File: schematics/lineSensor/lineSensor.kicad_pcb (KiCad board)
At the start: 2 copper layers, 27 parts, among them P1 CONN_01X01, P2 CONN_01X01, P3 CONN_01X01, P4 CONN_01X01, P5 CONN_01X01, P6 CONN_01X01, P7 CONN_01X01

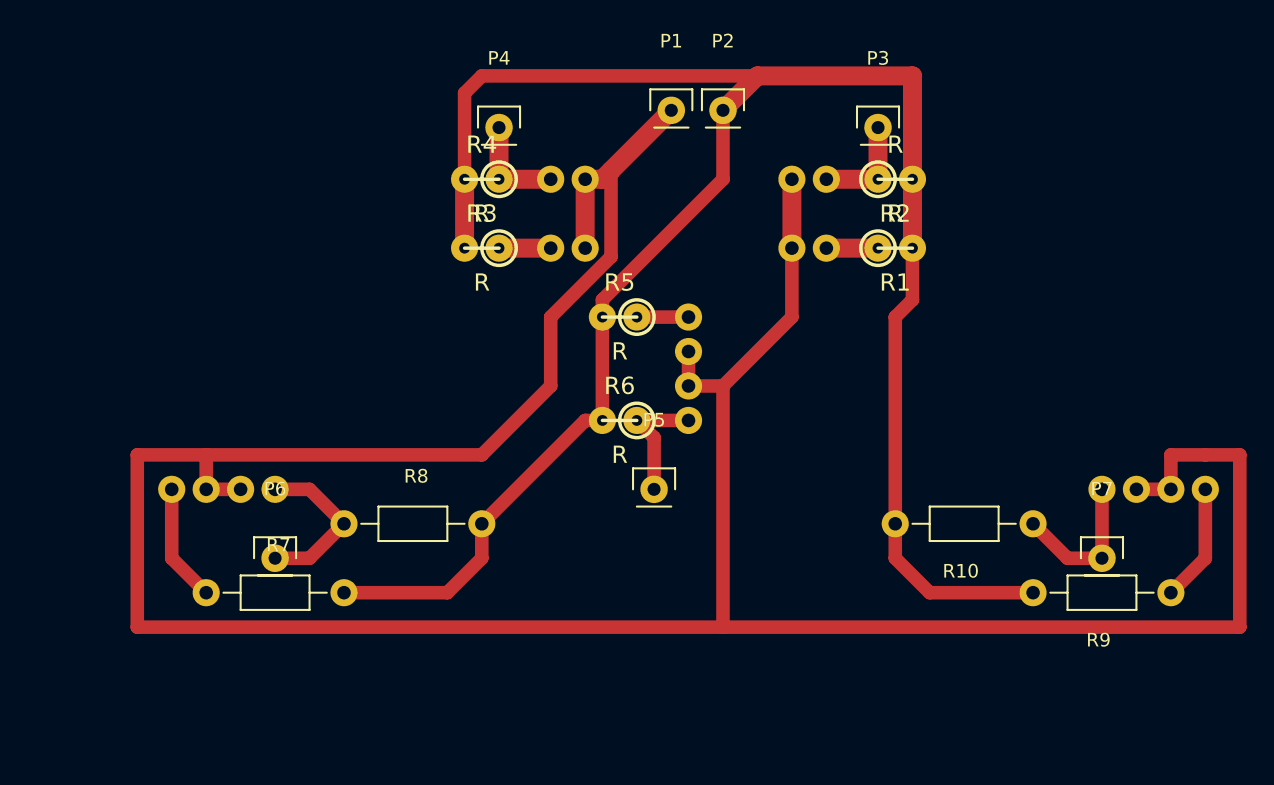
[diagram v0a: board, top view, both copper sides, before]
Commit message: Update schematic lineSensor and bug
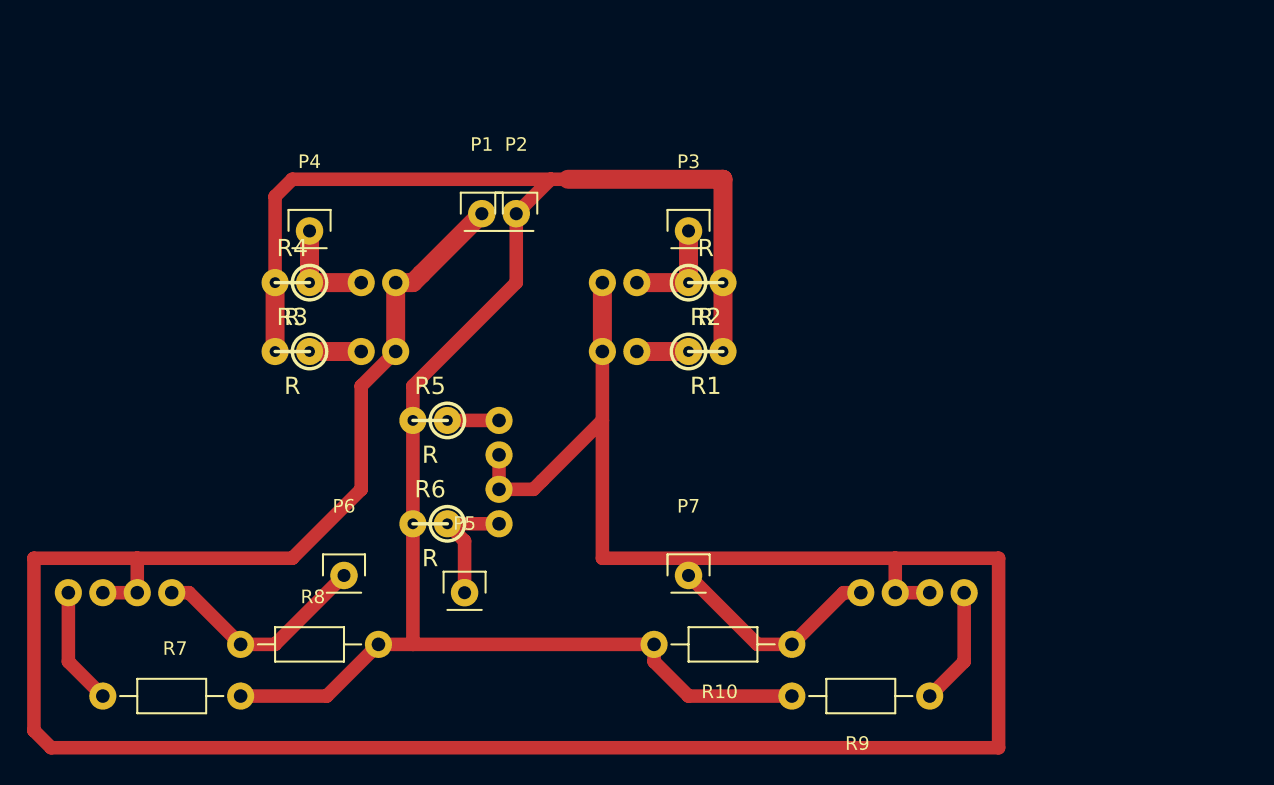
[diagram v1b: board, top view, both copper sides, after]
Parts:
- moved P7 30.5 mm to (157.5, 128.3)
- moved R10 19.9 mm to (165.1, 133.3)
- moved R9 19.3 mm to (175.3, 137.2)
- moved D10 19.3 mm to (170.2, 129.5)
- moved D9 19.3 mm to (177.8, 129.5)
- moved P2 17.0 mm to (144.8, 101.6)
- moved D1 15.9 mm to (153.7, 111.8)
- moved D2 15.9 mm to (153.7, 106.7)
- moved D3 15.9 mm to (133.3, 111.8)
- moved D4 15.9 mm to (133.3, 106.7)
- moved D5 15.9 mm to (143.5, 116.8)
- moved P3 15.9 mm to (157.5, 102.9)
- moved P4 15.9 mm to (129.5, 102.9)
- moved R1 15.9 mm to (158.8, 111.8)
- moved R2 15.9 mm to (158.8, 106.7)
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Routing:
- net Net-(P2-Pad1): track 148.2 -> 140.7 mm
- net Net-(D10-Pad1): track 11.2 -> 16.4 mm
- net Net-(D1-Pad2): track 226.0 -> 221.3 mm
- net Net-(D8-Pad1): track 12.3 -> 16.4 mm

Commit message: SCHEMATICS: group output pins
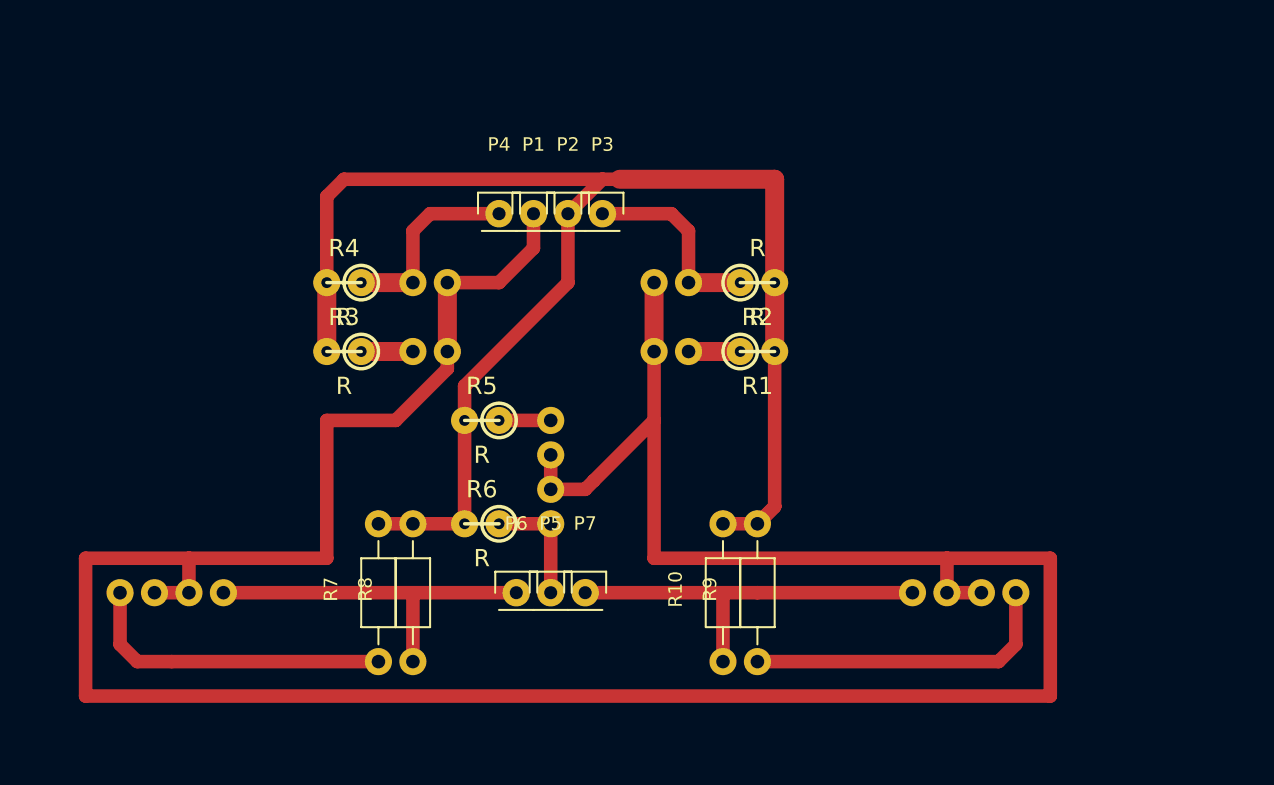
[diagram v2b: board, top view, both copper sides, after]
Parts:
- moved R7 20.5 mm to (134.6, 134.6), turned to 90 degrees
- moved P4 14.0 mm to (143.5, 101.6)
- moved R9 13.0 mm to (162.6, 134.6), turned to 90 degrees
- moved R8 12.8 mm to (137.2, 134.6), turned to 90 degrees
- moved P6 12.8 mm to (144.8, 129.5)
- moved P7 7.73 mm to (149.9, 129.5)
- moved P3 6.48 mm to (151.1, 101.6)
- moved P5 6.35 mm to (147.3, 129.5)
- moved R10 5.24 mm to (160.0, 134.6), turned to 90 degrees
- moved D1 3.81 mm to (157.5, 111.8)
- moved D10 3.81 mm to (174.0, 129.5)
- moved D2 3.81 mm to (157.5, 106.7)
- moved D3 3.81 mm to (137.2, 111.8)
- moved D4 3.81 mm to (137.2, 106.7)
- moved D5 3.81 mm to (147.3, 116.8)
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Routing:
- net Net-(P2-Pad1): track 140.7 -> 111.2 mm
- net Net-(D7-Pad1): track 8.67 -> 23.4 mm
- net Net-(D9-Pad1): track 8.67 -> 23.4 mm
- net Net-(D10-Pad1): track 16.4 -> 29.2 mm
- net Net-(D8-Pad1): track 16.4 -> 26.7 mm
- net Net-(D2-Pad1): track 7.62 -> 14.5 mm
- net Net-(D4-Pad1): track 7.62 -> 14.5 mm
- net Net-(D1-Pad2): track 221.3 -> 218.1 mm
- net Net-(D6-Pad1): track 9.42 -> 8.89 mm

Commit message: SCHEMATIC: update lineSensors and bug
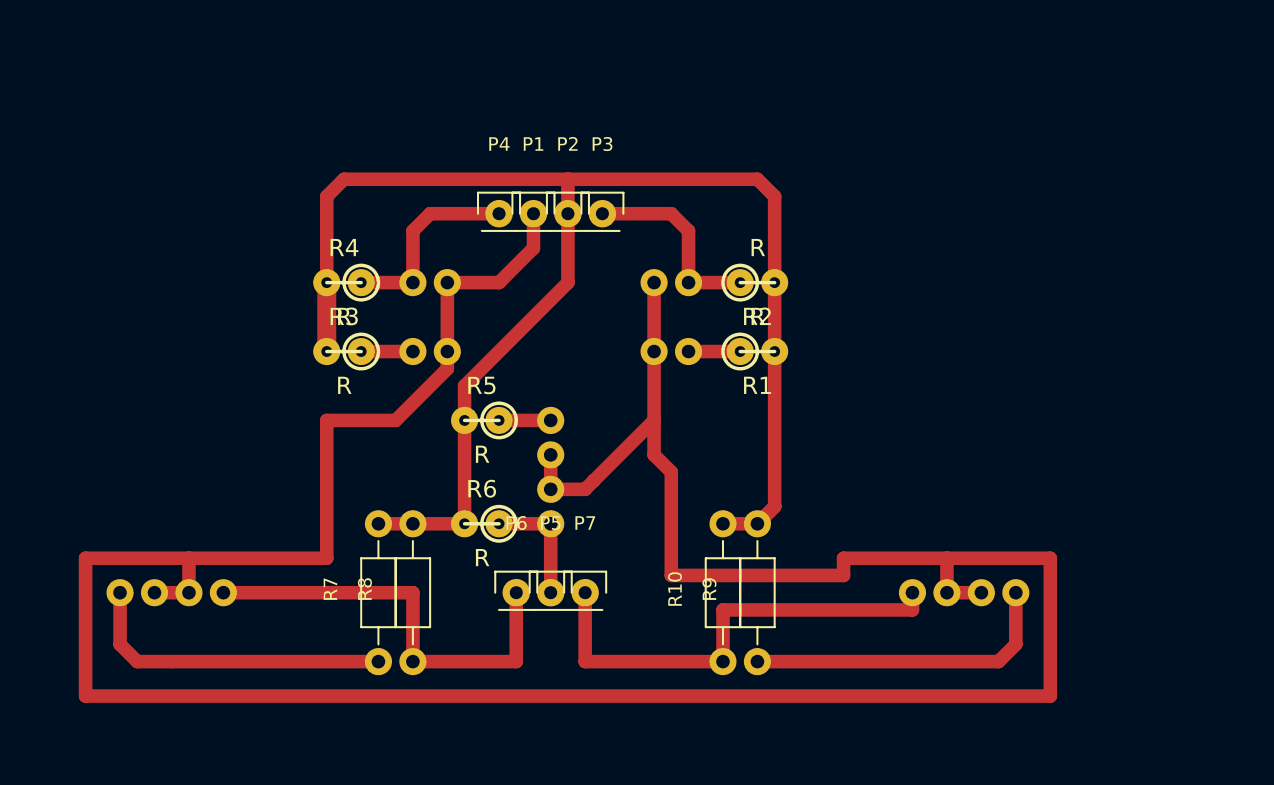
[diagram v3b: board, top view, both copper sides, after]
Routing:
- net Net-(D8-Pad1): track 26.7 -> 31.8 mm
- net Net-(D10-Pad1): track 29.2 -> 34.3 mm
- net Net-(D1-Pad2): track 218.1 -> 219.9 mm
- net Net-(P2-Pad1): track 111.2 -> 109.4 mm
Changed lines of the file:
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@@
     (links 35)
     (no_connects 0)
-    (area 106.579999 37.999999 182.980001 144.880001)
+    (area 110.389999 37.999999 186.790001 144.880001)
     (thickness 1.6)
     (drawings 7)
-    (tracks 72)
+    (tracks 81)
     (zones 0)
     (modules 27)
@@
     (last_trace_width 1)
     (user_trace_width 1)
+    (user_trace_width 1.9)
     (trace_clearance 0.2)
     (zone_clearance 0.508)
@@
   (gr_line (start 186.69 38.1) (end 186.69 82.55) (angle 90) (layer Eco1.User) (width 0.2))
   (gr_line (start 110.49 38.1) (end 186.69 38.1) (angle 90) (layer Eco1.User) (width 0.2))
-  (segment (start 161.29 111.76) (end 157.48 111.76) (width 1.4) (layer F.Cu) (net 1))
+  (segment (start 142.24 129.54) (end 142.24 129.54) (width 1.9) (layer F.Cu) (net 0))
+  (segment (start 142.24 129.54) (end 142.24 129.54) (width 1.9) (layer F.Cu) (net 0))
+  (segment (start 152.4 129.54) (end 152.4 129.54) (width 1.9) (layer F.Cu) (net 0))
+  (segment (start 161.29 111.76) (end 157.48 111.76) (width 1) (layer F.Cu) (net 1) (status C00000))
+  (segment (start 176.53 127) (end 168.91 127) (width 1) (layer F.Cu) (net 2))
+  (segment (start 154.94 119.38) (end 154.94 116.84) (width 1) (layer F.Cu) (net 2))
+  (segment (start 156.21 120.65) (end 154.94 119.38) (width 1) (layer F.Cu) (net 2))
+  (segment (start 156.21 128.27) (end 156.21 120.65) (width 1) (layer F.Cu) (net 2))
+  (segment (start 168.91 128.27) (end 156.21 128.27) (width 1) (layer F.Cu) (net 2))
+  (segment (start 168.91 127) (end 168.91 128.27) (width 1) (layer F.Cu) (net 2))
+  (segment (start 139.7 106.68) (end 139.7 111.76) (width 1) (layer F.Cu) (net 2) (status C00000))
+  (segment (start 154.94 106.68) (end 154.94 111.76) (width 1) (layer F.Cu) (net 2) (status C00000))
   (segment (start 176.53 127) (end 184.15 127) (width 1) (layer F.Cu) (net 2))
   (segment (start 113.03 127) (end 120.65 127) (width 1) (layer F.Cu) (net 2))
@@
   (segment (start 146.05 104.14) (end 143.51 106.68) (width 1) (layer F.Cu) (net 2))
   (segment (start 139.7 111.76) (end 139.7 113.03) (width 1) (layer F.Cu) (net 2))
+  (segment (start 130.81 127) (end 120.65 127) (width 1) (layer F.Cu) (net 2))
+  (segment (start 130.81 116.84) (end 130.81 127) (width 1) (layer F.Cu) (net 2))
+  (segment (start 135.89 116.84) (end 130.81 116.84) (width 1) (layer F.Cu) (net 2))
   (segment (start 139.7 113.03) (end 135.89 116.84) (width 1) (layer F.Cu) (net 2))
-  (segment (start 135.89 116.84) (end 130.81 116.84) (width 1) (layer F.Cu) (net 2))
-  (segment (start 130.81 116.84) (end 130.81 127) (width 1) (layer F.Cu) (net 2))
-  (segment (start 130.81 127) (end 120.65 127) (width 1) (layer F.Cu) (net 2))
-  (segment (start 176.53 127) (end 154.94 127) (width 1) (layer F.Cu) (net 2))
-  (segment (start 154.94 127) (end 154.94 116.84) (width 1) (layer F.Cu) (net 2))
   (segment (start 120.65 127) (end 120.65 129.54) (width 1) (layer F.Cu) (net 2))
   (segment (start 176.53 127) (end 176.53 129.54) (width 1) (layer F.Cu) (net 2))
   (segment (start 154.94 111.76) (end 154.94 116.84) (width 1) (layer F.Cu) (net 2))
   (segment (start 154.94 116.84) (end 150.495 121.285) (width 1) (layer F.Cu) (net 2))
+  (segment (start 150.495 121.285) (end 149.86 121.92) (width 1) (layer F.Cu) (net 2))
   (segment (start 149.86 121.92) (end 147.32 121.92) (width 1) (layer F.Cu) (net 2))
-  (segment (start 150.495 121.285) (end 149.86 121.92) (width 1) (layer F.Cu) (net 2))
   (segment (start 147.32 119.38) (end 147.32 121.92) (width 1) (layer F.Cu) (net 2))
   (segment (start 179.07 129.54) (end 176.53 129.54) (width 1) (layer F.Cu) (net 2))
   (segment (start 118.11 129.54) (end 120.65 129.54) (width 1) (layer F.Cu) (net 2))
-  (segment (start 154.94 111.76) (end 154.94 106.68) (width 1.4) (layer F.Cu) (net 2))
-  (segment (start 139.7 106.68) (end 139.7 111.76) (width 1.4) (layer F.Cu) (net 2))
+  (segment (start 157.48 106.68) (end 161.29 106.68) (width 1) (layer F.Cu) (net 3) (status C00000))
   (segment (start 157.48 106.68) (end 157.48 102.87) (width 1) (layer F.Cu) (net 3))
   (segment (start 156.21 101.6) (end 151.13 101.6) (width 1) (layer F.Cu) (net 3))
   (segment (start 157.48 102.87) (end 156.21 101.6) (width 1) (layer F.Cu) (net 3))
-  (segment (start 157.48 106.68) (end 161.29 106.68) (width 1.4) (layer F.Cu) (net 3))
-  (segment (start 133.35 111.76) (end 137.16 111.76) (width 1.4) (layer F.Cu) (net 4))
+  (segment (start 133.35 111.76) (end 137.16 111.76) (width 1) (layer F.Cu) (net 4) (status C00000))
+  (segment (start 137.16 106.68) (end 133.35 106.68) (width 1) (layer F.Cu) (net 5) (status C00000))
   (segment (start 137.16 106.68) (end 137.16 102.87) (width 1) (layer F.Cu) (net 5))
   (segment (start 138.43 101.6) (end 143.51 101.6) (width 1) (layer F.Cu) (net 5))
   (segment (start 137.16 102.87) (end 138.43 101.6) (width 1) (layer F.Cu) (net 5))
-  (segment (start 137.16 106.68) (end 133.35 106.68) (width 1.4) (layer F.Cu) (net 5))
   (segment (start 147.32 116.84) (end 143.51 116.84) (width 1) (layer F.Cu) (net 6))
   (segment (start 147.32 124.46) (end 147.32 129.54) (width 1) (layer F.Cu) (net 7))
@@
   (segment (start 116.84 134.62) (end 115.57 133.35) (width 1) (layer F.Cu) (net 8))
   (segment (start 119.38 134.62) (end 116.84 134.62) (width 1) (layer F.Cu) (net 8))
+  (segment (start 137.16 134.62) (end 144.78 134.62) (width 1) (layer F.Cu) (net 9))
+  (segment (start 144.78 134.62) (end 144.78 129.54) (width 1) (layer F.Cu) (net 9))
   (segment (start 137.16 129.54) (end 137.16 134.62) (width 1) (layer F.Cu) (net 9))
-  (segment (start 144.78 129.54) (end 137.16 129.54) (width 1) (layer F.Cu) (net 9))
   (segment (start 137.16 129.54) (end 123.19 129.54) (width 1) (layer F.Cu) (net 9))
   (segment (start 162.56 134.62) (end 180.34 134.62) (width 1) (layer F.Cu) (net 10))
   (segment (start 181.61 133.35) (end 181.61 129.54) (width 1) (layer F.Cu) (net 10))
   (segment (start 180.34 134.62) (end 181.61 133.35) (width 1) (layer F.Cu) (net 10))
-  (segment (start 160.02 129.54) (end 160.02 134.62) (width 1) (layer F.Cu) (net 11))
-  (segment (start 162.56 129.54) (end 160.02 129.54) (width 1) (layer F.Cu) (net 11))
-  (segment (start 160.02 129.54) (end 149.86 129.54) (width 1) (layer F.Cu) (net 11))
-  (segment (start 173.99 129.54) (end 162.56 129.54) (width 1) (layer F.Cu) (net 11))
+  (segment (start 160.02 134.62) (end 160.02 130.81) (width 1) (layer F.Cu) (net 11) (status 400000))
+  (segment (start 173.99 130.81) (end 173.99 129.54) (width 1) (layer F.Cu) (net 11) (status 800000))
+  (segment (start 160.02 130.81) (end 173.99 130.81) (width 1) (layer F.Cu) (net 11))
+  (segment (start 149.86 129.54) (end 149.86 134.62) (width 1) (layer F.Cu) (net 11))
+  (segment (start 149.86 134.62) (end 160.02 134.62) (width 1) (layer F.Cu) (net 11))
+  (segment (start 163.83 106.68) (end 163.83 111.76) (width 1) (layer F.Cu) (net 12) (status C00000))
+  (segment (start 148.59 99.06) (end 162.56 99.06) (width 1) (layer F.Cu) (net 12))
+  (segment (start 163.83 100.33) (end 163.83 106.68) (width 1) (layer F.Cu) (net 12) (status 800000))
+  (segment (start 162.56 99.06) (end 163.83 100.33) (width 1) (layer F.Cu) (net 12))
+  (segment (start 148.59 101.6) (end 148.59 99.06) (width 1) (layer F.Cu) (net 12) (status 400000))
+  (segment (start 130.81 106.68) (end 130.81 100.33) (width 1) (layer F.Cu) (net 12))
+  (segment (start 130.81 100.33) (end 132.08 99.06) (width 1) (layer F.Cu) (net 12))
+  (segment (start 132.08 99.06) (end 148.59 99.06) (width 1) (layer F.Cu) (net 12))
   (segment (start 162.56 124.46) (end 160.02 124.46) (width 1) (layer F.Cu) (net 12))
   (segment (start 163.83 111.76) (end 163.83 123.19) (width 1) (layer F.Cu) (net 12))
@@
   (segment (start 163.83 123.19) (end 162.56 124.46) (width 1) (layer F.Cu) (net 12))
   (segment (start 140.97 124.46) (end 140.97 116.84) (width 1) (layer F.Cu) (net 12))
-  (segment (start 148.59 101.6) (end 151.13 99.06) (width 1) (layer F.Cu) (net 12))
   (segment (start 148.59 101.6) (end 148.59 106.68) (width 1) (layer F.Cu) (net 12))
   (segment (start 140.97 114.3) (end 140.97 116.84) (width 1) (layer F.Cu) (net 12))
   (segment (start 148.59 106.68) (end 140.97 114.3) (width 1) (layer F.Cu) (net 12))
-  (segment (start 130.81 106.68) (end 130.81 100.33) (width 1) (layer F.Cu) (net 12))
-  (segment (start 130.81 100.33) (end 132.08 99.06) (width 1) (layer F.Cu) (net 12))
-  (segment (start 132.08 99.06) (end 151.13 99.06) (width 1) (layer F.Cu) (net 12))
-  (segment (start 151.13 99.06) (end 152.4 99.06) (width 1) (layer F.Cu) (net 12))
-  (segment (start 152.4 99.06) (end 163.83 99.06) (width 1.4) (layer F.Cu) (net 12))
-  (segment (start 163.83 106.68) (end 163.83 99.06) (width 1.4) (layer F.Cu) (net 12))
-  (segment (start 163.83 106.68) (end 163.83 111.76) (width 1.4) (layer F.Cu) (net 12))
   (segment (start 130.81 111.76) (end 130.81 106.68) (width 1.4) (layer F.Cu) (net 12))
 )
